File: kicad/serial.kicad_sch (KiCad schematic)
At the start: 13 parts, among them J7 DE9_Plug_MountingHoles, J8 USB_C_Receptacle_USB2.0_14P, U25 MAX232, U26 CH340N

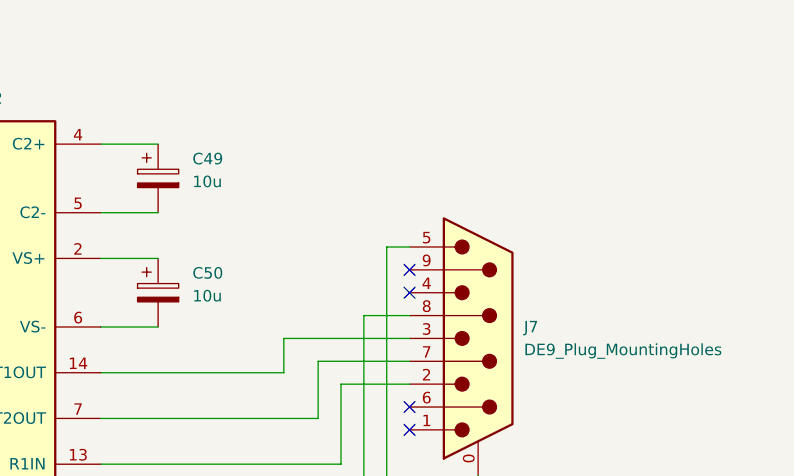
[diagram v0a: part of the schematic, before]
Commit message: HW: Fix unconnected /SOUND net, add /RST header and /DTR power supply
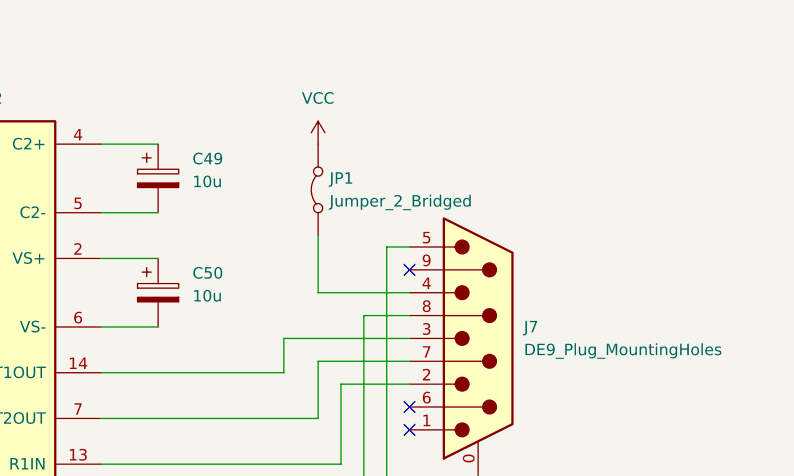
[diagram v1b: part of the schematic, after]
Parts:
- added JP1: Jumper_2_Bridged, Jumper:SolderJumper-2_P1.3mm_Bridged_Pad1.0x1.5mm, symbol Jumper:Jumper_2_Bridged
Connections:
- net VCC: now also JP1.2 (B)
- net at J7.4: now also JP1.1 (A)
- no-connect marks 5 -> 4
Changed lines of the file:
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@@
-	)
-	(no_connect
-		(at 179.07 62.23)
 	)
 	(no_connect
@@
 	(wire
 		(pts
+			(xy 179.07 62.23) (xy 168.91 62.23)
+		)
+		(stroke
+			(width 0)
+			(type default)
+		)
+	)
+	(wire
+		(pts
 			(xy 176.53 90.17) (xy 176.53 86.36)
 		)
@@
 		(pts
 			(xy 80.01 133.35) (xy 77.47 133.35)
+		)
+		(stroke
+			(width 0)
+			(type default)
+		)
+	)
+	(wire
+		(pts
+			(xy 168.91 62.23) (xy 168.91 55.88)
 		)
 		(stroke
@@
 	)
 	(symbol
+		(lib_id "Jumper:Jumper_2_Bridged")
+		(at 168.91 50.8 90)
+		(unit 1)
+		(exclude_from_sim yes)
+		(in_bom yes)
+		(on_board yes)
+		(dnp no)
+		(fields_autoplaced yes)
+		(property "Reference" "JP1"
+			(at 170.18 49.5299 90)
+			(effects
+				(font
+					(size 1.27 1.27)
+				)
+				(justify right)
+			)
+		)
+		(property "Value" "Jumper_2_Bridged"
+			(at 170.18 52.0699 90)
+			(effects
+				(font
+					(size 1.27 1.27)
+				)
+				(justify right)
+			)
+		)
+		(property "Footprint" "Jumper:SolderJumper-2_P1.3mm_Bridged_Pad1.0x1.5mm"
+			(at 168.91 50.8 0)
+			(effects
+				(font
+					(size 1.27 1.27)
+				)
+				(hide yes)
+			)
+		)
+		(property "Datasheet" "~"
+			(at 168.91 50.8 0)
+			(effects
+				(font
+					(size 1.27 1.27)
+				)
+				(hide yes)
+			)
+		)
+		(property "Description" "Jumper, 2-pole, closed/bridged"
+			(at 168.91 50.8 0)
+			(effects
+				(font
+					(size 1.27 1.27)
+				)
+				(hide yes)
+			)
+		)
+		(pin "1"
+		)
+		(pin "2"
+		)
+		(instances
+			(project ""
+				(path "/ca48b56d-33a4-442b-b1b9-aaf2c2c8d68d/516e3187-6836-4ba1-8de7-3bdb26e69da6"
+					(reference "JP1")
+					(unit 1)
+				)
+			)
+		)
+	)
+	(symbol
 		(lib_id "Device:C_Polarized")
 		(at 151.13 49.53 0)
@@
 					(unit 1)
 				)
+			)
+		)
+	)
+	(symbol
+		(lib_id "power:VCC")
+		(at 168.91 45.72 0)
+		(unit 1)
+		(exclude_from_sim no)
+		(in_bom yes)
+		(on_board yes)
+		(dnp no)
+		(fields_autoplaced yes)
+		(property "Reference" "#PWR0193"
+			(at 168.91 49.53 0)
+			(effects
+				(font
+					(size 1.27 1.27)
+				)
+				(hide yes)
+			)
+		)
+		(property "Value" "VCC"
+			(at 168.91 40.64 0)
+			(effects
+				(font
+					(size 1.27 1.27)
+				)
+			)
+		)
+		(property "Footprint" ""
+			(at 168.91 45.72 0)
+			(effects
+				(font
+					(size 1.27 1.27)
+				)
+				(hide yes)
+			)
+		)
+		(property "Datasheet" ""
+			(at 168.91 45.72 0)
+			(effects
+				(font
+					(size 1.27 1.27)
+				)
+				(hide yes)
+			)
+		)
+		(property "Description" "Power symbol creates a global label with name \"VCC\""
+			(at 168.91 45.72 0)
+			(effects
+				(font
+					(size 1.27 1.27)
+				)
+				(hide yes)
+			)
+		)
+		(pin "1"
+		)
+		(instances
+			(project "zak180"
+				(path "/ca48b56d-33a4-442b-b1b9-aaf2c2c8d68d/516e3187-6836-4ba1-8de7-3bdb26e69da6"
+					(reference "#PWR0193")
+					(unit 1)
+				)
